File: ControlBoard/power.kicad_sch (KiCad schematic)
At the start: 29 parts, among them Q1 PMOS, U2 AP63205WU, U3 AP2112K-3.3

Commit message: WIP: placement
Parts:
- BAU1, C_BATT1: footprint Connector_PinHeader_2.54mm:PinHeader_1x02_P2.54mm_Vertical -> Connector_AMASS:AMASS_XT30U-M_1x02_P5.0mm_Vertical
- C10: renamed from C1; footprint (none) -> Capacitor_SMD:C_0603_1608Metric
- C11: renamed from C3; footprint (none) -> Capacitor_SMD:C_0603_1608Metric
- C5: renamed from C19; footprint lib:CAP_EEETC1C101V -> Capacitor_SMD:CP_Elec_10x14.3
- F1: footprint Package_LCC:PLCC-84_29.3x29.3mm_P1.27mm -> Fuse:Fuse_0603_1608Metric
- Q1: footprint Package_DIP:DIP-24_W7.62mm -> Package_TO_SOT_SMD:SOT-223
- R5: renamed from R3; footprint Package_DIP:DIP-8_W7.62mm -> Resistor_SMD:R_0603_1608Metric
- renumbered U2 to BUCK1, C11 to C4, C2 to C6, C6 to C7, C7 to C8, C8 to C9, JP2 to JP1, JP3 to JP2, L2 to L1, U3 to LDO1, S_3.3V to LED_3.3V1, S_5V to LED_5V1, S_BATT to LED_BATT1, R5 to R3, R6 to R4, R10 to R6, R11 to R7, R12 to R8, TP2 to TP1, TP3 to TP2, TP4 to TP3
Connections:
- net at R5.1: now also Q1.1 (G); no longer Q1.2 (G)
- net at F1.2: now also Q1.2 (D); no longer Q1.1 (D)

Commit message: Feat: multiplex power over usb + add gitignore
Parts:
- added D1, D2: D_Schottky, Diode_SMD:D_0603_1608Metric, symbol Device:D_Schottky
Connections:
- net +5V: now also D1.1 (K), D2.1 (K); no longer JP1.2 (B)
- new net: D1.2 (A), JP1.2 (B)
- new net USB: D2.2 (A)
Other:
- moved on the sheet: C10, C11, JP2, LDO1

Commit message: fix: a lot of small things, simplify
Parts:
- C10, C11: value 0.1uF -> 1uF
- R3: value 20K -> 30K
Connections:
- net +5V: now also D1.2 (A), JP1.2 (B); no longer C10.1, D1.1 (K), D2.1 (K), LDO1.1 (VIN), LDO1.3 (EN)
- new net: C10.1, D1.1 (K), D2.1 (K), LDO1.1 (VIN), LDO1.3 (EN)

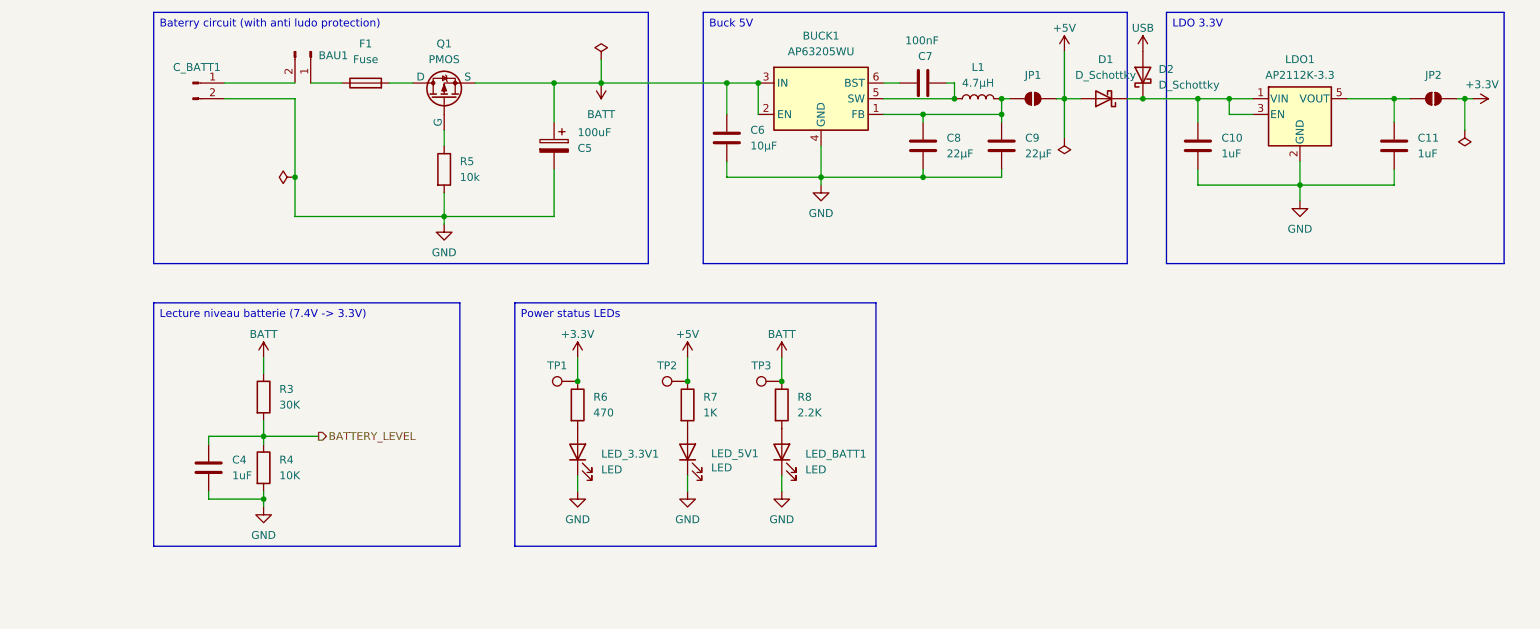
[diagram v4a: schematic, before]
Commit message: (change): buck 2A -> 3A (from 63200 to 63300)
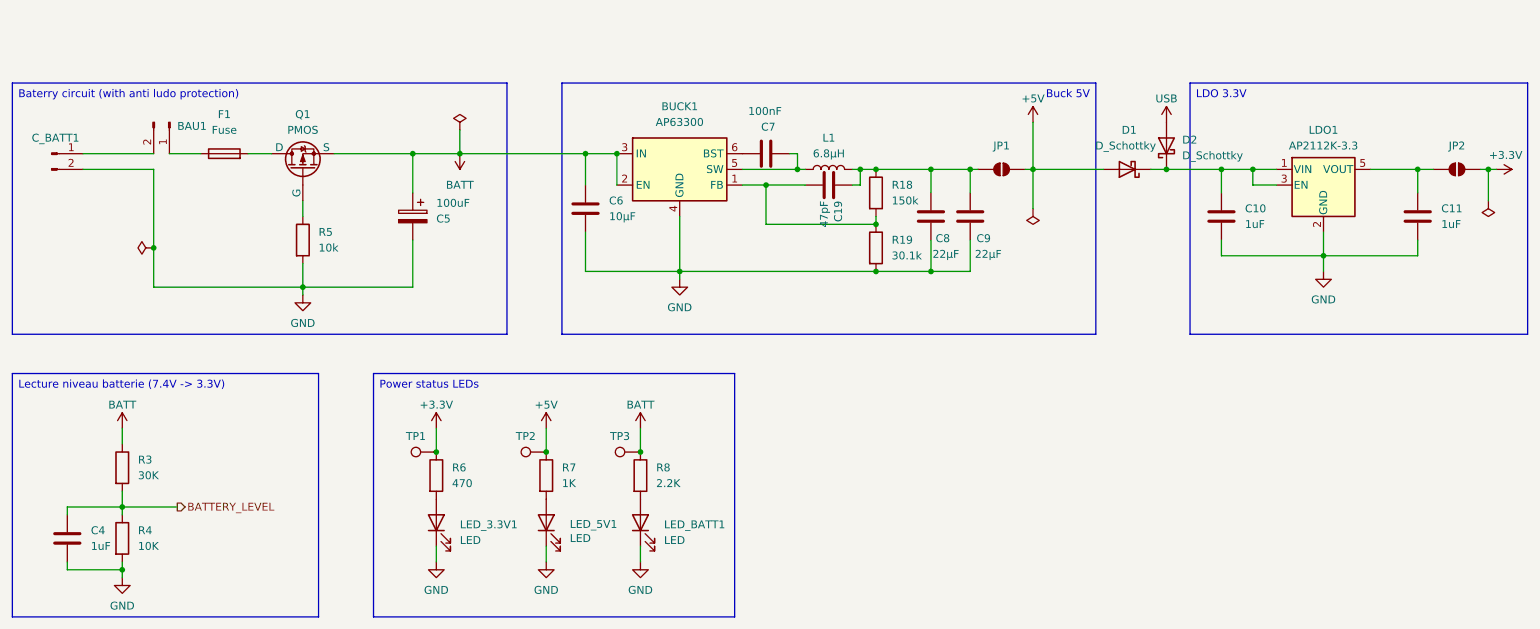
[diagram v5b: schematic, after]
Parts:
- added C19: 47pF, Capacitor_SMD:C_0402_1005Metric, symbol Device:C
- added R18: 150k, PCM_SparkFun-Resistor:R_0603_1608Metric, symbol Device:R
- added R19: 30.1k, PCM_SparkFun-Resistor:R_0603_1608Metric, symbol Device:R
- BUCK1: value AP63205WU -> AP63300; LCSC C2071056 -> C2158012
- L1: value 4.7µH -> 6.8µH
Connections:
- net GND: now also R19.2
- net at C8.1, C9.1, JP1.1 (A)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: now also C19.1, R18.1; no longer BUCK1.1 (FB)
- new net: BUCK1.1 (FB), C19.2, R18.2, R19.1
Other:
- moved on the sheet: BAU1, BUCK1, C10, C11, C4, C5, C6, C7, C8, C9, C_BATT1, D1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

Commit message: (feat): bom
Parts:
- C10, C11: LCSC (none) -> C1592
- D1, D2: LCSC (none) -> C153761
- F1: LCSC (none) -> C52988540
- L1: LCSC C6364810 -> C5349706
- LDO1: LCSC (none) -> C51118
- Q1: LCSC (none) -> C179617
- R18: LCSC (none) -> C114660
- R19: LCSC (none) -> C137745
- R4: LCSC C98220 -> C84376
- R5: LCSC (none) -> C84376
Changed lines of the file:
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@@
 			)
 		)
+		(property "LCSC" "C84376"
+			(at 69.85 78.74 0)
+			(hide yes)
+			(show_name no)
+			(do_not_autoplace no)
+			(effects
+				(font
+					(size 1.27 1.27)
+				)
+			)
+		)
 		(pin "1"
 		)
@@
 			)
 		)
+		(property "LCSC" "C1592"
+			(at 250.19 74.93 0)
+			(hide yes)
+			(show_name no)
+			(do_not_autoplace no)
+			(effects
+				(font
+					(size 1.27 1.27)
+				)
+			)
+		)
 		(pin "1"
 		)
@@
 			)
 		)
+		(property "LCSC" "C51118"
+			(at 234.95 69.85 0)
+			(hide yes)
+			(show_name no)
+			(do_not_autoplace no)
+			(effects
+				(font
+					(size 1.27 1.27)
+				)
+			)
+		)
 		(pin "2"
 		)
@@
 			)
 		)
+		(property "LCSC" "C52988540"
+			(at 57.15 64.77 90)
+			(hide yes)
+			(show_name no)
+			(do_not_autoplace no)
+			(effects
+				(font
+					(size 1.27 1.27)
+				)
+			)
+		)
 		(pin "2"
 		)
@@
 			)
 		)
+		(property "LCSC" "C153761"
+			(at 203.2 67.31 0)
+			(hide yes)
+			(show_name no)
+			(do_not_autoplace no)
+			(effects
+				(font
+					(size 1.27 1.27)
+				)
+			)
+		)
 		(pin "1"
 		)
@@
 			)
 		)
+		(property "LCSC" "C114660"
+			(at 162.56 71.12 0)
+			(hide yes)
+			(show_name no)
+			(do_not_autoplace no)
+			(effects
+				(font
+					(size 1.27 1.27)
+				)
+			)
+		)
 		(pin "1"
 		)
@@
 			)
 		)
+		(property "LCSC" "C179617"
+			(at 69.85 67.31 90)
+			(hide yes)
+			(show_name no)
+			(do_not_autoplace no)
+			(effects
+				(font
+					(size 1.27 1.27)
+				)
+			)
+		)
 		(pin "3"
 		)
@@
 			)
 		)
+		(property "LCSC" "C137745"
+			(at 162.56 80.01 0)
+			(hide yes)
+			(show_name no)
+			(do_not_autoplace no)
+			(effects
+				(font
+					(size 1.27 1.27)
+				)
+			)
+		)
 		(pin "2"
 		)
@@
 			)
 		)
+		(property "LCSC" "C1592"
+			(at 218.44 74.93 0)
+			(hide yes)
+			(show_name no)
+			(do_not_autoplace no)
+			(effects
+				(font
+					(size 1.27 1.27)
+				)
+			)
+		)
 		(pin "1"
 		)
@@
 			)
 		)
-		(property "LCSC" "C6364810"
+		(property "LCSC" "C5349706"
 			(at 154.94 67.31 90)
 			(hide yes)
@@
 			)
 		)
-		(property "LCSC" "C98220"
+		(property "LCSC" "C84376"
 			(at 40.64 127 0)
 			(hide yes)
@@
 			(hide yes)
 			(show_name no)
+			(do_not_autoplace no)
+			(effects
+				(font
+					(size 1.27 1.27)
+				)
+			)
+		)
+		(property "LCSC" "C153761"
+			(at 209.55 63.5 90)
+			(hide yes)
+			(show_name no)

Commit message: (feat): routing v2
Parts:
- C19: footprint Capacitor_SMD:C_0402_1005Metric -> Capacitor_SMD:C_0805_2012Metric; LCSC C602037 -> C107118
- C7: footprint Capacitor_SMD:C_0603_1608Metric -> Capacitor_SMD:C_0805_2012Metric; LCSC C1591 -> C49678
- R18: footprint PCM_SparkFun-Resistor:R_0603_1608Metric -> Resistor_SMD:R_0805_2012Metric; LCSC C114660 -> C2907299
- R19: footprint PCM_SparkFun-Resistor:R_0603_1608Metric -> Resistor_SMD:R_0805_2012Metric; LCSC C137745 -> C5184185
- R5: footprint Resistor_SMD:R_0603_1608Metric -> Resistor_SMD:R_0805_2012Metric
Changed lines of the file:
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@@
 			)
 		)
-		(property "Footprint" "Resistor_SMD:R_0603_1608Metric"
+		(property "Footprint" "Resistor_SMD:R_0805_2012Metric"
 			(at 68.072 78.74 90)
 			(hide yes)
@@
 			)
 		)
-		(property "Footprint" "Capacitor_SMD:C_0402_1005Metric"
+		(property "Footprint" "Capacitor_SMD:C_0805_2012Metric"
 			(at 151.13 70.8152 0)
 			(hide yes)
@@
 			)
 		)
-		(property "LCSC" "C602037"
+		(property "LCSC" "C107118"
 			(at 154.94 69.85 0)
 			(hide yes)
@@
 			)
 		)
-		(property "Footprint" "Capacitor_SMD:C_0603_1608Metric"
+		(property "Footprint" "Capacitor_SMD:C_0805_2012Metric"
 			(at 148.59 63.8048 0)
 			(hide yes)
@@
 			)
 		)
-		(property "LCSC" "C1591"
+		(property "LCSC" "C49678"
 			(at 144.78 64.77 90)
 			(hide yes)
@@
 			)
 		)
-		(property "Footprint" "PCM_SparkFun-Resistor:R_0603_1608Metric"
+		(property "Footprint" "Resistor_SMD:R_0805_2012Metric"
 			(at 160.782 71.12 90)
 			(hide yes)
@@
 			)
 		)
-		(property "LCSC" "C114660"
+		(property "LCSC" "C2907299"
 			(at 162.56 71.12 0)
 			(hide yes)
@@
 			)
 		)
-		(property "Footprint" "PCM_SparkFun-Resistor:R_0603_1608Metric"
+		(property "Footprint" "Resistor_SMD:R_0805_2012Metric"
 			(at 160.782 80.01 90)
 			(hide yes)
@@
 			)
 		)
-		(property "LCSC" "C137745"
+		(property "LCSC" "C5184185"
 			(at 162.56 80.01 0)
 			(hide yes)

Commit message: Updates to schematic by Ludo <3
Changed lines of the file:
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@@
 	(wire
 		(pts
-			(xy 261.62 67.31) (xy 261.62 72.39)
+			(xy 261.62 67.31) (xy 261.62 68.58)
 		)
 		(stroke
@@
 	(wire
 		(pts
-			(xy 187.96 59.69) (xy 187.96 67.31)
+			(xy 187.96 64.77) (xy 187.96 67.31)
 		)
 		(stroke
@@
 	(wire
 		(pts
-			(xy 187.96 67.31) (xy 187.96 73.66)
+			(xy 187.96 67.31) (xy 187.96 68.58)
 		)
 		(stroke
@@
 		)
 	)
+	(netclass_flag ""
+		(length 2.54)
+		(shape round)
+		(at 54.61 86.36 0)
+		(fields_autoplaced yes)
+		(effects
+			(font
+				(size 1.27 1.27)
+			)
+			(justify left bottom)
+		)
+		(property "Netclass" "GND"
+			(at 55.3085 83.82 0)
+			(show_name no)
+			(do_not_autoplace no)
+			(effects
+				(font
+					(size 1.27 1.27)
+				)
+				(justify left)
+			)
+		)
+		(property "Component Class" "GND"
+			(at 55.3085 85.2805 0)
+			(hide yes)
+			(show_name no)
+			(do_not_autoplace no)
+			(effects
+				(font
+					(size 1.27 1.27)
+					(italic yes)
+				)
+				(justify left)
+			)
+		)
+	)
 	(symbol
 		(lib_id "PCM_SparkFun-PowerSymbol:VCC")
@@
 		(property "Value" "GND"
 			(at 124.46 135.382 0)
+			(hide yes)
 			(show_name no)
 			(do_not_autoplace no)
@@
 		(lib_id "Device:C")
 		(at 154.94 69.85 270)
+		(mirror x)
 		(unit 1)
 		(body_style 1)
@@
 		(dnp no)
 		(property "Reference" "C19"
-			(at 156.464 72.39 0)
+			(at 154.94 77.47 90)
 			(show_name no)
 			(do_not_autoplace no)
@@
 					(size 1.27 1.27)
 				)
-				(justify left)
 			)
 		)
 		(property "Value" "47pF"
-			(at 154.178 72.39 0)
+			(at 154.94 74.93 90)
 			(show_name no)
 			(do_not_autoplace no)
@@
 					(size 1.27 1.27)
 				)
-				(justify left)
 			)
 		)
 		(property "Footprint" "Capacitor_SMD:C_0805_2012Metric"
-			(at 151.13 70.8152 0)
+			(at 151.13 68.8848 0)
 			(hide yes)
 			(show_name no)
@@
 		(property "Value" "GND"
 			(at 40.64 137.922 0)
+			(hide yes)
 			(show_name no)
 			(do_not_autoplace no)
@@
 		(property "Value" "GND"
 			(at 130.81 89.662 0)
+			(hide yes)
 			(show_name no)
 			(do_not_autoplace no)
@@
 	(symbol
 		(lib_id "power:PWR_FLAG")
-		(at 261.62 72.39 180)
+		(at 261.62 68.58 180)
 		(unit 1)
 		(body_style 1)
@@
 		(fields_autoplaced yes)
 		(property "Reference" "#FLG04"
-			(at 261.62 74.295 0)
+			(at 261.62 70.485 0)
 			(hide yes)
 			(show_name no)
@@
 		)
 		(property "Value" "PWR_FLAG"
-			(at 261.6201 76.2 90)
+			(at 261.6201 72.39 90)
 			(hide yes)
 			(show_name no)
@@
 		)
 		(property "Footprint" ""
-			(at 261.62 72.39 0)
+			(at 261.62 68.58 0)
 			(hide yes)
 			(show_name no)
@@
 		)
 		(property "Datasheet" ""
-			(at 261.62 72.39 0)
+			(at 261.62 68.58 0)
 			(hide yes)
 			(show_name no)
@@
 		)
 		(property "Description" "Special symbol for telling ERC where power comes from"
-			(at 261.62 72.39 0)
+			(at 261.62 68.58 0)
 			(hide yes)
 			(show_name no)
@@
 		(property "Value" "GND"
 			(at 109.22 135.382 0)
+			(hide yes)
 			(show_name no)
 			(do_not_autoplace no)
@@
 		(property "Value" "GND"
 			(at 91.44 135.382 0)
+			(hide yes)
 			(show_name no)
 			(do_not_autoplace no)
@@
 		(property "Value" "GND"
 			(at 234.95 88.392 0)
+			(hide yes)
 			(show_name no)
 			(do_not_autoplace no)
@@
 		(in_pos_files yes)
 		(dnp no)
+		(fields_autoplaced yes)
 		(property "Reference" "D1"
-			(at 203.5175 60.96 0)
+			(at 203.5175 71.12 0)
 			(show_name no)
 			(do_not_autoplace no)
@@
 		)
 		(property "Value" "D_Schottky"
-			(at 202.946 63.5 0)
+			(at 203.5175 73.66 0)
 			(show_name no)
 			(do_not_autoplace no)
@@
 		(property "Value" "GND"
 			(at 69.85 92.202 0)
+			(hide yes)
 			(show_name no)
 			(do_not_autoplace no)
@@
 	(symbol
 		(lib_id "PCM_SparkFun-PowerSymbol:VCC")
-		(at 187.96 59.69 0)
+		(at 187.96 64.77 0)
 		(unit 1)
 		(body_style 1)
@@
 		(fields_autoplaced yes)
 		(property "Reference" "#PWR016"
-			(at 187.96 63.5 0)
+			(at 187.96 68.58 0)
 			(hide yes)
 			(show_name no)
@@
 		)
 		(property "Value" "+5V"
-			(at 187.96 55.88 0)
+			(at 187.96 60.96 0)
 			(show_name no)
 			(do_not_autoplace yes)
@@
 		)
 		(property "Footprint" ""
-			(at 187.96 59.69 0)
+			(at 187.96 64.77 0)
 			(hide yes)
 			(show_name no)
@@
 		)
 		(property "Datasheet" ""
-			(at 187.96 59.69 0)
+			(at 187.96 64.77 0)
 			(hide yes)
 			(show_name no)
@@
 		)
 		(property "Description" "Power symbol creates a global label with name \"VCC\""
-			(at 187.96 66.04 0)
+			(at 187.96 71.12 0)
 			(hide yes)
 			(show_name no)
@@
 		(in_pos_files yes)
 		(dnp no)
+		(fields_autoplaced yes)
 		(property "Reference" "C5"
-			(at 91.44 75.3111 0)
+			(at 91.44 72.7709 0)
 			(show_name no)
 			(do_not_autoplace no)
@@
 		)
 		(property "Value" "100uF"
-			(at 91.44 72.7711 0)
+			(at 91.44 75.3109 0)
 			(show_name no)
 			(do_not_autoplace no)
@@
 	(symbol
 		(lib_id "power:PWR_FLAG")
-		(at 187.96 73.66 180)
+		(at 187.96 68.58 180)
 		(unit 1)
 		(body_style 1)
@@
 		(fields_autoplaced yes)
 		(property "Reference" "#FLG03"
-			(at 187.96 75.565 0)
+			(at 187.96 70.485 0)
 			(hide yes)
 			(show_name no)
@@
 		)
 		(property "Value" "PWR_FLAG"
-			(at 187.9601 77.47 90)
+			(at 187.9601 72.39 90)
 			(hide yes)
 			(show_name no)
@@
 		)
 		(property "Footprint" ""
-			(at 187.96 73.66 0)
+			(at 187.96 68.58 0)
 			(hide yes)
 			(show_name no)
@@
 		)
 		(property "Datasheet" ""
-			(at 187.96 73.66 0)
+			(at 187.96 68.58 0)
 			(hide yes)
 			(show_name no)
@@
 		)
 		(property "Description" "Special symbol for telling ERC where power comes from"
-			(at 187.96 73.66 0)
+			(at 187.96 68.58 0)
 			(hide yes)
 			(show_name no)
